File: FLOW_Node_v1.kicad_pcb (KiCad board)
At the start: 2 copper layers, 84 x 60 mm, 36 parts, among them J1 Conn_01x04_Pin, J5 Conn_02x05_Odd_Even, J7 Conn_01x04_Pin, J8 Conn_01x02, J9 Conn_01x02, U1 STM32L053R8Tx, U2 MAX7375AXR805

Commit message: Updated Node PCB
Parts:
- J5: footprint Connector_PinHeader_2.54mm:PinHeader_1x05_P2.54mm_Vertical -> Connector_PinHeader_2.54mm:PinHeader_2x05_P2.54mm_Vertical
- moved J7 75.5 mm to (65.0, 64.0)
- moved D1 38.5 mm to (114.9, 54.5)
- moved D2 38.5 mm to (114.9, 59.0)
- moved D3 38.5 mm to (114.9, 63.5)
- moved D4 38.5 mm to (114.9, 68.0)
- moved R3 38.5 mm to (120.1, 55.0)
- moved R4 38.5 mm to (120.1, 59.0)
- moved R5 38.5 mm to (119.9, 63.5)
- moved R6 38.5 mm to (120.0, 68.0)
- moved J5 32.3 mm to (76.4, 34.0)
- moved R9 30.0 mm to (92.5, 67.0)
- moved D5 27.1 mm to (84.0, 37.5), turned to -90 degrees
- moved J1 7.65 mm to (65.0, 48.0), turned to -90 degrees
- moved R7 3.50 mm to (98.0, 48.0)
- moved C2 3.04 mm to (100.5, 67.0)
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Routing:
- net GND: track 0.00 -> 183.1 mm
- net /NRST: track 0.00 -> 144.6 mm
- net /Battery: track 0.00 -> 105.6 mm
- net /SWDIO_IN: track 0.00 -> 78.3 mm
- net +3V3: track 0.00 -> 41.3 mm
- net +3.3V: track 0.00 -> 40.7 mm
- net /Ultrasonic_TX: track 0.00 -> 40.5 mm
- net /Ultrasonic_RX: track 0.00 -> 40.5 mm
- net /LORA_RX: track 0.00 -> 37.8 mm
- net /SWCLK_IN: track 0.00 -> 36.3 mm
- net /PC1_LED: track 0.00 -> 28.5 mm
- net /PC3_LED: track 0.00 -> 28.3 mm
- net /PC0_LED: track 0.00 -> 27.1 mm
- net /PC2_LED: track 0.00 -> 26.6 mm
- net Net-(D1-A): track 0.00 -> 7.28 mm
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
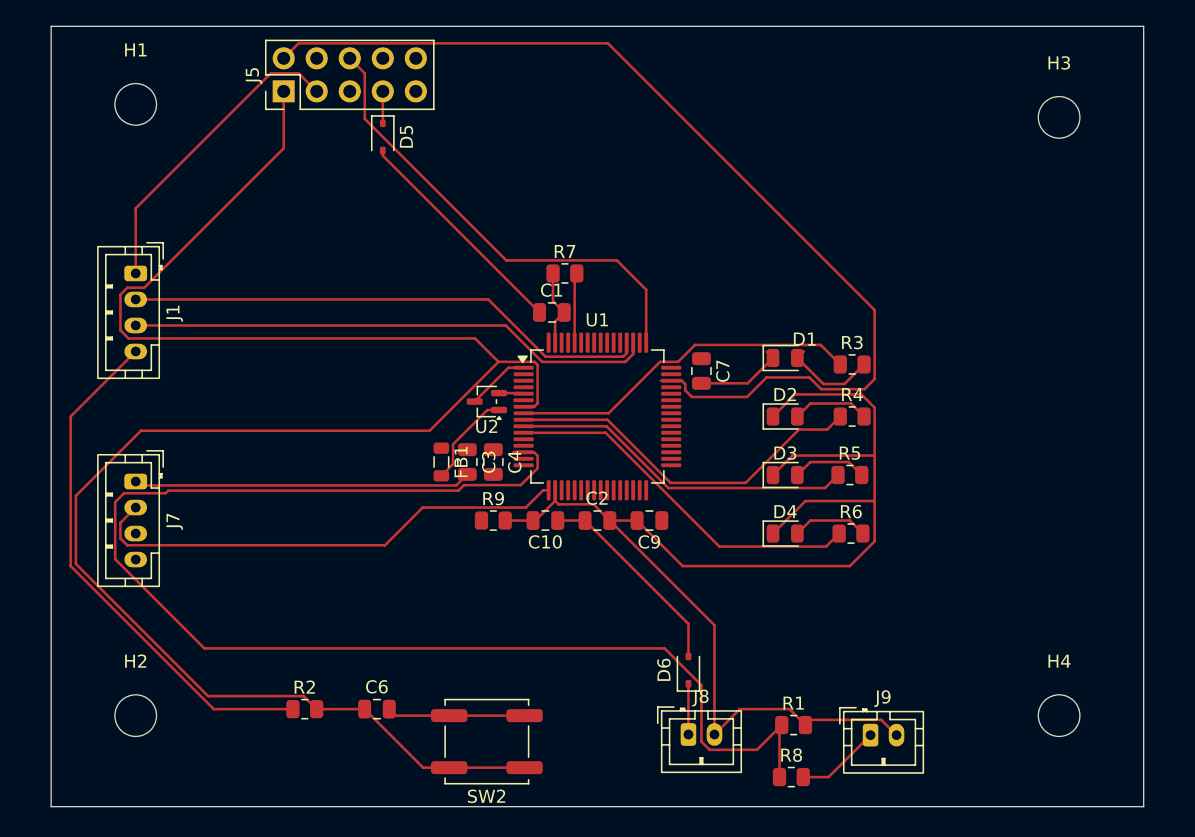
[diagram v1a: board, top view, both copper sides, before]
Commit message: Newest Node PCB
with ground plane
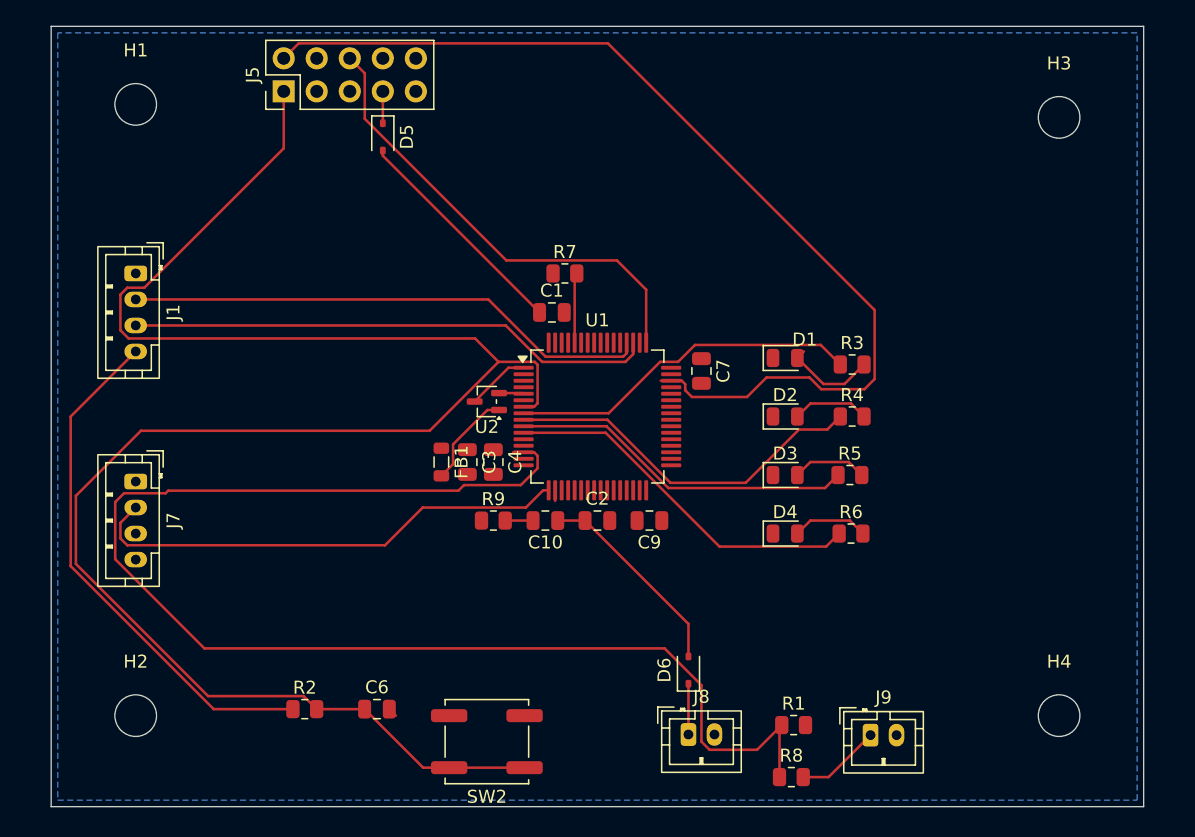
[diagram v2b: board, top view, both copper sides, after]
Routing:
- net GND: track 183.1 -> 9.67 mm
- added copper zone on B.Cu, net GND
